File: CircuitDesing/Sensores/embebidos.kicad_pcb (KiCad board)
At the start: 2 copper layers, 7 parts, among them U1 ESP32-WROOM-32

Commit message: Huellas
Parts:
- removed REF** (x2): JST_XH_S3B-XH-A-1_1x03_P2.50mm_Horizontal, Connector_JST:JST_XH_S3B-XH-A-1_1x03_P2.50mm_Horizontal
- added C4: 1uF, Capacitor_SMD:C_0603_1608Metric_Pad1.08x0.95mm_HandSolder, F.Cu at (96.5, 100.3)
- added DHT11_1: Conn_01x03, Connector_JST:JST_EH_B3B-EH-A_1x03_P2.50mm_Vertical, F.Cu at (82.5, 104.1)
- added DHT11_2: Conn_01x03, Connector_JST:JST_EH_B3B-EH-A_1x03_P2.50mm_Vertical, F.Cu at (68.0, 115.8)
- added HC-SR04_0: Conn_01x04, Connector_JST:JST_EH_B4B-EH-A_1x04_P2.50mm_Vertical, F.Cu at (68.0, 104.1)
- added HMI1: Conn_01x07, Connector_JST:JST_EH_B7B-EH-A_1x07_P2.50mm_Vertical, F.Cu at (105.4, 124.5)
- added I2C1: Conn_01x03, Connector_JST:JST_EH_B3B-EH-A_1x03_P2.50mm_Vertical, F.Cu at (117.5, 136.2)
- added J1: Conn_01x02, TerminalBlock:TerminalBlock_bornier-2_P5.08mm, F.Cu at (72.8, 92.5)
- added R2: 2k, Resistor_SMD:R_0603_1608Metric_Pad0.98x0.95mm_HandSolder, F.Cu at (96.5, 89.3)
- added R3: 10k, Resistor_SMD:R_0603_1608Metric_Pad0.98x0.95mm_HandSolder, F.Cu at (96.5, 102.8)
- added REED1: Conn_01x02, Connector_JST:JST_EH_B2B-EH-A_1x02_P2.50mm_Vertical, F.Cu at (80.0, 110.0)
- added RIEGO1: Conn_01x06, Connector_JST:JST_EH_B6B-EH-A_1x06_P2.50mm_Vertical, F.Cu at (105.4, 130.3)
- added SE093_1: Conn_01x03, Connector_JST:JST_EH_B3B-EH-A_1x03_P2.50mm_Vertical, F.Cu at (68.0, 110.0)
- added SW1: SW_Push, Button_Switch_SMD:SW_Push_1P1T_NO_6x6mm_H9.5mm, F.Cu at (81.3, 128.3)
- added SW2: SW_Push, Button_Switch_SMD:SW_Push_1P1T_NO_6x6mm_H9.5mm, F.Cu at (70.0, 128.6)
- added U2: AMS1117-3.3, Package_TO_SOT_SMD:SOT-223-3_TabPin2, F.Cu at (86.0, 92.2)
- added VENTILACION1: Conn_01x03, Connector_JST:JST_EH_B3B-EH-A_1x03_P2.50mm_Vertical, F.Cu at (105.4, 136.2)
- moved C1 46.5 mm to (105.4, 86.8), turned to 90 degrees
- moved C2 30.0 mm to (110.5, 86.4), turned to 90 degrees
- moved U1 15.3 mm to (123.2, 91.6)
- moved C3 12.5 mm to (143.5, 82.5)
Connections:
- net +3.3V renamed /3.3v
- U1 pad 10: unconnected-(U1-Pad10) -> /ControlV1
- U1 pad 11: unconnected-(U1-Pad11) -> /ConrolV2
- U1 pad 12: unconnected-(U1-Pad12) -> /ControlV3
- U1 pad 13: unconnected-(U1-Pad13) -> /Buzzer
- U1 pad 14: unconnected-(U1-Pad14) -> /Izquierda
- U1 pad 16: unconnected-(U1-Pad16) -> /Centro
- U1 pad 23: unconnected-(U1-Pad23) -> /hc_0_trig
- U1 pad 24: unconnected-(U1-Pad24) -> /Arriba
- U1 pad 25: unconnected-(U1-Pad25) -> /Esp32Schematic/BOOT
- U1 pad 26: unconnected-(U1-Pad26) -> /Abajo
- U1 pad 27: unconnected-(U1-Pad27) -> /hc_0_echo
- U1 pad 28: unconnected-(U1-Pad28) -> /dht11_1d
- U1 pad 29: unconnected-(U1-Pad29) -> /Derecha
- U1 pad 30: unconnected-(U1-Pad30) -> /dht11_2d
- U1 pad 31: unconnected-(U1-Pad31) -> /lm393_1_d
- U1 pad 33: unconnected-(U1-Pad33) -> /SDA
- U1 pad 34: unconnected-(U1-Pad34) -> /Esp32Schematic/RXD0/IO3
- U1 pad 35: unconnected-(U1-Pad35) -> /Esp32Schematic/TXD0/IO1
- U1 pad 36: unconnected-(U1-Pad36) -> /SCL
- U1 pad 37: unconnected-(U1-Pad37) -> /REED
- U1 pad 6: unconnected-(U1-Pad6) -> /C_hum
- U1 pad 7: unconnected-(U1-Pad7) -> /C_temp
- U1 pad 8: unconnected-(U1-Pad8) -> /ControlV4
- U1 pad 9: unconnected-(U1-Pad9) -> /Control_V5
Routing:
- net /3.3v: track 108.0 -> 0.07 mm
- net GND: track 68.3 -> 0.00 mm

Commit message: Ruteo listo
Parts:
- added Iluminación1: Conn_01x03, Connector_JST:JST_EH_B3B-EH-A_1x03_P2.50mm_Vertical, F.Cu at (112.5, 154.4)
- added JI2C2: Conn_01x04, Connector_JST:JST_EH_B4B-EH-A_1x04_P2.50mm_Vertical, F.Cu at (79.1, 153.9)
- added J_I2C1: Conn_01x05_Male, Connector_PinSocket_2.54mm:PinSocket_1x05_P2.54mm_Horizontal, F.Cu at (77.3, 78.5)
- added J_prog1: Conn_01x06_Male, Connector_PinHeader_2.54mm:PinHeader_1x06_P2.54mm_Horizontal, F.Cu at (143.7, 75.7)
- added L_p1: LED, LED_SMD:LED_0805_2012Metric_Pad1.15x1.40mm_HandSolder, F.Cu at (97.5, 98.0)
- added RCL1: 10k, Resistor_SMD:R_0805_2012Metric_Pad1.20x1.40mm_HandSolder, F.Cu at (92.7, 128.5)
- added RCL2: 10k, Resistor_SMD:R_0805_2012Metric_Pad1.20x1.40mm_HandSolder, F.Cu at (93.0, 133.3)
- added RCL3: 10k, Resistor_SMD:R_0805_2012Metric_Pad1.20x1.40mm_HandSolder, F.Cu at (102.6, 118.9)
- added RDA1: 10k, Resistor_SMD:R_0805_2012Metric_Pad1.20x1.40mm_HandSolder, F.Cu at (102.6, 114.0)
- added RDA2: 10k, Resistor_SMD:R_0805_2012Metric_Pad1.20x1.40mm_HandSolder, F.Cu at (102.6, 124.2)
- added RDA3: 10k, Resistor_SMD:R_0805_2012Metric_Pad1.20x1.40mm_HandSolder, F.Cu at (99.1, 107.4)
- added R_p1: 47, Resistor_SMD:R_0805_2012Metric_Pad1.20x1.40mm_HandSolder, F.Cu at (102.9, 100.3)
- moved DHT11_2 80.7 mm to (143.5, 144.3), turned to 90 degrees
- moved REED1 63.7 mm to (143.8, 111.0), turned to 90 degrees
- moved DHT11_1 62.2 mm to (144.3, 97.1), turned to -90 degrees
- moved BOOT1 60.9 mm to (129.5, 115.6), turned to -90 degrees
- moved Temp&Humi1 42.8 mm to (143.5, 155.7), turned to 90 degrees
- moved C3 42.2 mm to (103.3, 95.2)
- moved R2 41.9 mm to (138.4, 87.6)
- moved C4 39.7 mm to (136.1, 101.9)
- moved HMI1 39.1 mm to (143.7, 132.5), turned to 90 degrees
- moved EN1 39.0 mm to (118.1, 115.6), turned to -90 degrees
- moved R3 36.6 mm to (133.1, 104.6)
- moved R1 31.9 mm to (104.1, 90.2)
- moved RIEGO1 26.5 mm to (93.3, 153.9)
- moved J1 23.3 mm to (86.4, 73.7)
- moved I2C1 19.3 mm to (123.7, 154.4)
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- renumbered SW2 to BOOT1, SW1 to EN1, VENTILACION1 to Temp&Humi1
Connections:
- net /Control_V5 renamed /ControlV5
- C1 pad 1: /3.3v -> 3.3v
- C2 pad 1: /3.3v -> 3.3v
- DHT11_1 pad 1: /5v -> 3.3v
- DHT11_2 pad 1: /5v -> 3.3v
- HC-SR04_0 pad 1: /5v -> 5v
- J1 pad 1: /5v -> 5v
- R1 pad 1: /3.3v -> 3.3v
- R3 pad 1: GND -> 3.3v
- REED1 pad 1: /5v -> 3.3v
- SE093_1 pad 1: /5v -> 3.3v
- SE093_1 pad 2: /Sensores/SE093_1_D -> /lm393_1_D
- U1 pad 14: /Izquierda -> /C_temp
- U1 pad 2: /3.3v -> 3.3v
- U1 pad 29: /Derecha -> /C_hum
- U1 pad 31: /lm393_1_d -> /lm393_1_D
- U1 pad 33: /SDA -> SDA
- U1 pad 34: /Esp32Schematic/RXD0/IO3 -> /Prog_Tx
- U1 pad 35: /Esp32Schematic/TXD0/IO1 -> /Prog_Rx
- U1 pad 36: /SCL -> SCL
- U1 pad 5: unconnected-(U1-Pad5) -> /LedU1
- U1 pad 6: /C_hum -> /Derecha
- U1 pad 7: /C_temp -> /Izquierda
- U2 pad 2: /3.3v -> 3.3v
- U2 pad 3: /5v -> 5v
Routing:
- net 3.3v: track 0.00 -> 282.2 mm, vias 0 -> 8
- net GND: track 0.00 -> 281.9 mm, vias 0 -> 2
- net SDA: track 0.00 -> 192.7 mm, vias 0 -> 5
- net SCL: track 0.00 -> 172.4 mm, vias 0 -> 2
- net /C_temp: track 0.00 -> 73.4 mm
- net /ControlV4: track 0.00 -> 73.0 mm
- net /dht11_2d: track 0.00 -> 72.6 mm, vias 0 -> 2
- net /ControlV5: track 0.00 -> 72.4 mm, vias 0 -> 1
- net /C_hum: track 0.00 -> 71.0 mm, vias 0 -> 3
- net /hc_0_echo: track 0.00 -> 69.8 mm, vias 0 -> 4
- net /hc_0_trig: track 0.00 -> 68.7 mm, vias 0 -> 3
- net /lm393_1_D: track 0.00 -> 67.9 mm, vias 0 -> 2
- net /Izquierda: track 0.00 -> 67.3 mm, vias 0 -> 2
- net /ControlV1: track 0.00 -> 66.5 mm
- net /ConrolV2: track 0.00 -> 66.2 mm, vias 0 -> 1
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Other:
- board text added: "3.3V"
- board text added: "5V"
- board text added: "GND"
- board text added: "NO SEEEE CONECTAAAA"
- board text added: "RX"
- board text added: "SCL"
- board text added: "SDA"
- board text added: "TX"
- board text added: "Toca conectar estos dos puntos ??"

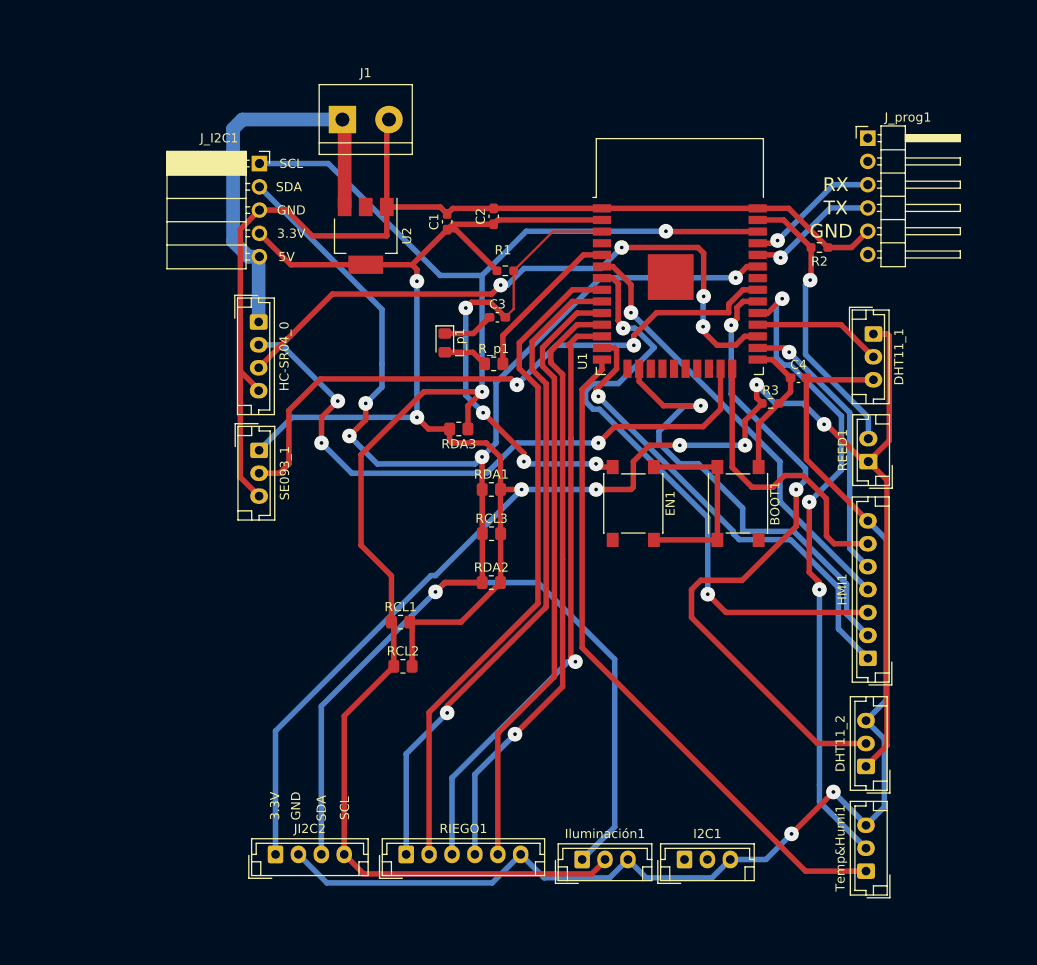
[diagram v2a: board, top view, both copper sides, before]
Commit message: Arreglo error de ruteo
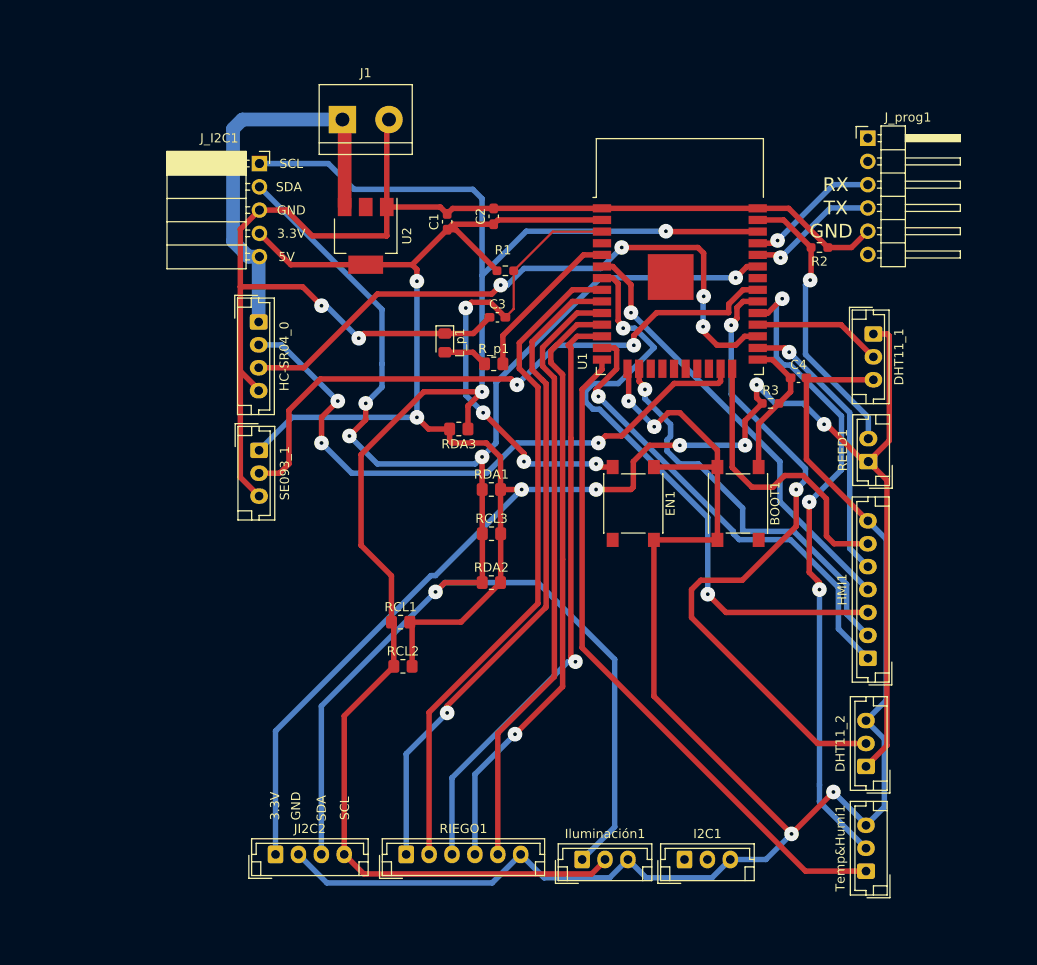
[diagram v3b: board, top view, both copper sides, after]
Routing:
- net GND: track 281.9 -> 363.6 mm, vias 2 -> 6
- net /Centro: track 51.1 -> 44.2 mm
- net SCL: track 172.4 -> 177.3 mm
- net /hc_0_trig: track 68.7 -> 66.9 mm

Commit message: Ruteo2.0
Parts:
- removed HC-SR04_0: Conn_01x04, Connector_JST:JST_EH_B4B-EH-A_1x04_P2.50mm_Vertical
- removed HMI1: Conn_01x07, Connector_JST:JST_EH_B7B-EH-A_1x07_P2.50mm_Vertical
- removed I2C1, Temp&Humi1: Conn_01x03, Connector_JST:JST_EH_B3B-EH-A_1x03_P2.50mm_Vertical
- removed J_prog1: Conn_01x06_Male, Connector_PinHeader_2.54mm:PinHeader_1x06_P2.54mm_Horizontal
- removed RCL3, RDA3: 10k, Resistor_SMD:R_0805_2012Metric_Pad1.20x1.40mm_HandSolder
- added Botones_M1: Conn_01x03, Connector_JST:JST_EH_B3B-EH-A_1x03_P2.50mm_Vertical, F.Cu at (68.8, 118.9)
- added Buzzer1: Conn_01x02, Connector_JST:JST_EH_B2B-EH-A_1x02_P2.50mm_Vertical, F.Cu at (68.9, 101.1)
- added C-Actuadores1: Conn_01x05, Connector_JST:JST_EH_B5B-EH-A_1x05_P2.50mm_Vertical, F.Cu at (129.5, 156.5)
- added C5: 10u, Capacitor_SMD:C_0603_1608Metric_Pad1.08x0.95mm_HandSolder, F.Cu at (81.0, 94.0)
- added C6: 100u, Capacitor_SMD:C_0603_1608Metric_Pad1.08x0.95mm_HandSolder, F.Cu at (83.8, 94.0)
- added HC-SR1: Conn_01x04, Connector_JST:JST_EH_B4B-EH-A_1x04_P2.50mm_Vertical, F.Cu at (143.8, 136.4)
- added J1: Conn_01x03_Male, Connector_PinHeader_2.54mm:PinHeader_1x03_P2.54mm_Vertical, F.Cu at (144.3, 94.8)
- added LedRojo1: Conn_01x02, Connector_JST:JST_EH_B2B-EH-A_1x02_P2.50mm_Vertical, F.Cu at (68.8, 110.0)
- added LedVerde1: Conn_01x02, Connector_JST:JST_EH_B2B-EH-A_1x02_P2.50mm_Vertical, F.Cu at (143.7, 145.3)
- added Q1: BSS138, Package_TO_SOT_SMD:SOT-23, F.Cu at (95.0, 97.3)
- added Q2: BSS138, Package_TO_SOT_SMD:SOT-23, F.Cu at (117.9, 109.5)
- added Q3: BSS138, Package_TO_SOT_SMD:SOT-23, F.Cu at (126.2, 109.5)
- added R4: 10k, Resistor_SMD:R_0603_1608Metric_Pad0.98x0.95mm_HandSolder, F.Cu at (120.9, 109.5)
- added R5: 10k, Resistor_SMD:R_0603_1608Metric_Pad0.98x0.95mm_HandSolder, F.Cu at (116.8, 114.6)
- added R6: 10k, Resistor_SMD:R_0603_1608Metric_Pad0.98x0.95mm_HandSolder, F.Cu at (129.3, 109.5)
- added R7: 10k, Resistor_SMD:R_0603_1608Metric_Pad0.98x0.95mm_HandSolder, F.Cu at (125.2, 114.6)
- added R_p2: 47, Resistor_SMD:R_0805_2012Metric_Pad1.20x1.40mm_HandSolder, F.Cu at (133.9, 145.0)
- added R_p3: 1k, Resistor_SMD:R_0805_2012Metric_Pad1.20x1.40mm_HandSolder, F.Cu at (77.0, 107.4)
- added Rb1: 1k, Resistor_SMD:R_0603_1608Metric_Pad0.98x0.95mm_HandSolder, F.Cu at (99.1, 98.3)
- moved BOOT1 45.6 mm to (144.3, 72.4), turned to 90 degrees
- moved EN1 41.6 mm to (101.3, 77.5)
- moved DHT11_2 33.3 mm to (143.7, 111.0)
- moved Iluminación1 29.7 mm to (82.8, 156.4)
- moved R2 26.0 mm to (142.0, 80.3)
- moved DHT11_1 25.3 mm to (143.7, 122.4), turned to 90 degrees
- moved C4 23.6 mm to (145.8, 80.3)
- moved REED1 22.6 mm to (143.7, 88.4)
- moved SE093_1 22.2 mm to (68.9, 130.3)
- moved R_p1 18.5 mm to (85.3, 106.2)
- moved L_p1 18.4 mm to (81.5, 107.2), turned to 90 degrees
- moved RIEGO1 17.2 mm to (110.3, 156.4)
- moved JI2C1 15.7 mm to (94.5, 156.4)
- moved C3 10.9 mm to (108.7, 84.1)
- moved RCL2 9.43 mm to (93.7, 124.0)
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- renumbered C3 to C1, C1 to C3, J1 to J2, JI2C2 to JI2C1, R3 to R2, R2 to R3
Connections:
- U1 pad 10: /ControlV1 -> /ControlV3
- U1 pad 12: /ControlV3 -> /ControlV1
- U1 pad 14: /C_temp -> /C_ilum
- U1 pad 16: /Centro -> /C_temp1
- U1 pad 23: /hc_0_trig -> /Trig
- U1 pad 24: /Arriba -> /Echo
- U1 pad 26: /Abajo -> /C_temp2
- U1 pad 27: /hc_0_echo -> /Led_Verde
- U1 pad 31: /lm393_1_D -> /Esp32Schematic/IO19
- U1 pad 6: /Derecha -> /Botones
- U1 pad 7: /Izquierda -> /lm393_1_D
- U1 pad 8: /ControlV4 -> /ControlV5
- U1 pad 9: /ControlV5 -> /ControlV4
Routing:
- net 5v: track 45.0 -> 156.9 mm, vias 0 -> 5
- net /C_temp2: track 0.00 -> 88.5 mm, vias 0 -> 2
- net /C_temp: track 73.4 -> 0.00 mm
- net /C_temp1: track 0.00 -> 71.2 mm
- net /hc_0_echo: track 69.8 -> 0.00 mm, vias 4 -> 0
- net /C_ilum: track 0.00 -> 68.4 mm
- net /Izquierda: track 67.3 -> 0.00 mm, vias 2 -> 0
- net /hc_0_trig: track 66.9 -> 0.00 mm, vias 3 -> 0
- net /Botones: track 0.00 -> 61.3 mm
- net /Led_Verde: track 0.00 -> 60.1 mm, vias 0 -> 2
- net /dht11_2d: track 72.6 -> 20.9 mm, vias 2 -> 0
- net /Derecha: track 48.0 -> 0.00 mm, vias 1 -> 0
- net /Centro: track 44.2 -> 0.00 mm, vias 1 -> 0
- net /Sensores/Conversor_NLog5/HV1: track 0.00 -> 39.5 mm
- net Net-(Buzzer1-Pad2): track 0.00 -> 38.8 mm
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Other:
- board text removed: "NO SEEEE CONECTAAAA"
- board text removed: "Toca conectar estos dos puntos ??"
